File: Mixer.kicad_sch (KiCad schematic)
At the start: 5 parts, among them IC1 ADE-2ASK+, J1 PCB.SMAFRA.HT, J2 PCB.SMAFRA.HT, J3 PCB.SMAFRA.HT

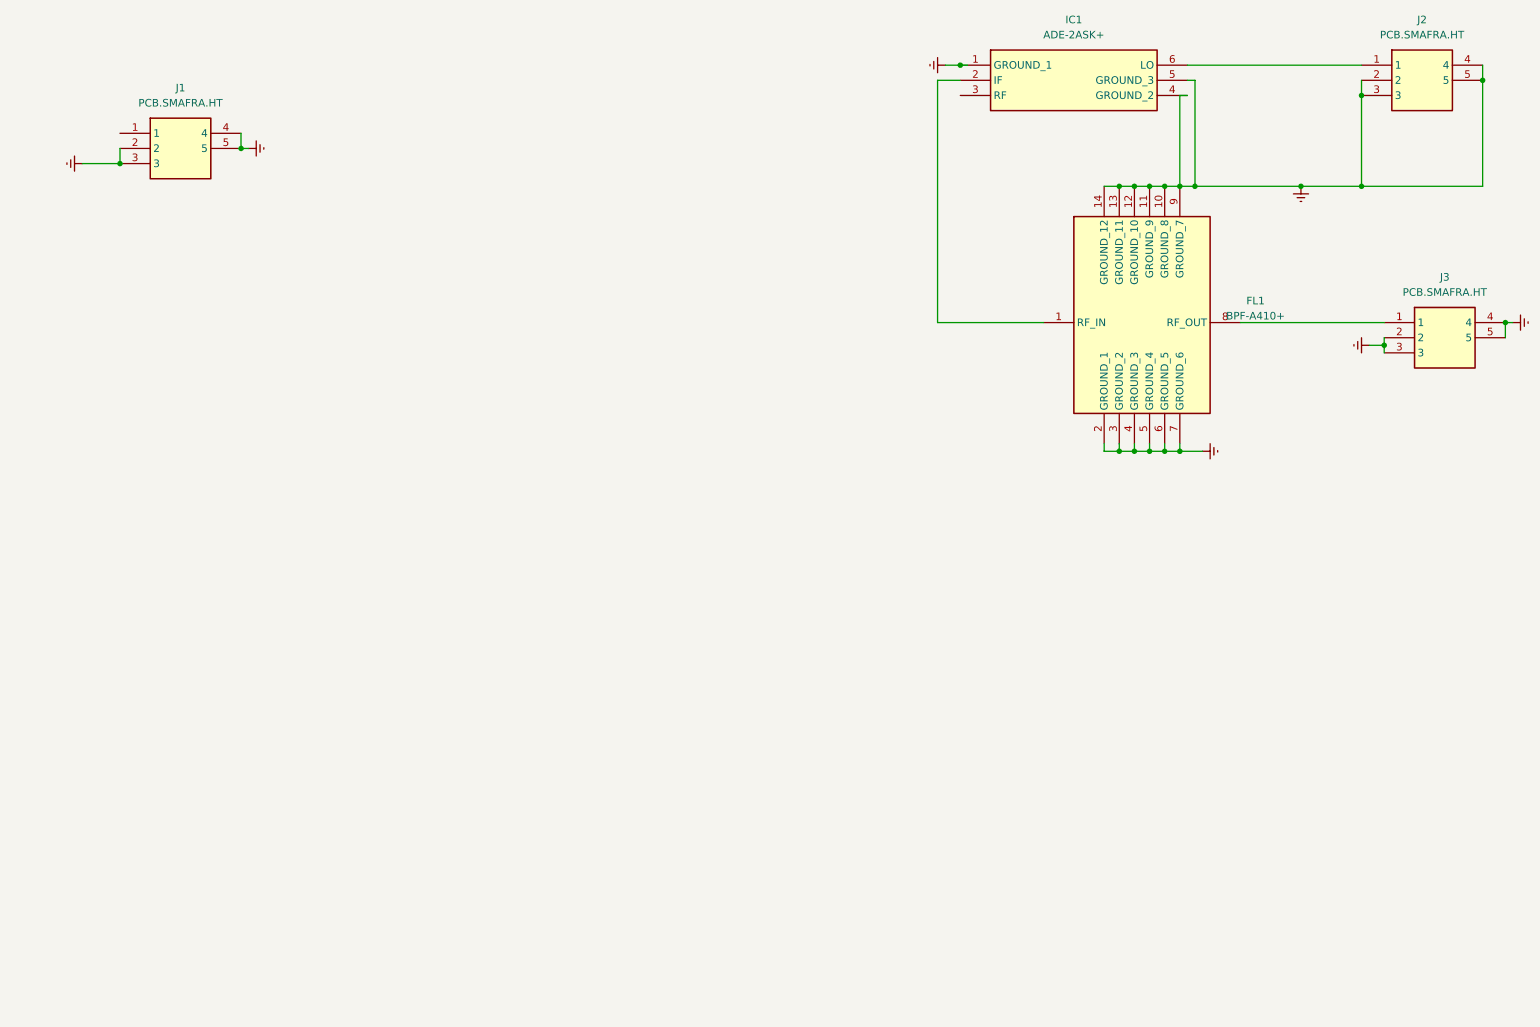
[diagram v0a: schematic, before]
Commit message: Redefined filters & Top Level Diagram
- Implement wider filters to accomodate 10% tolerance parts.
- Break design in to top-level heirarchical blocks.
- Start wiring some of the blocks together.
- Add L-Band segment, but is currently just a copy of the UHF filter.
- Add the start of a TX path.
- Add placeholders for power and band/tune control.
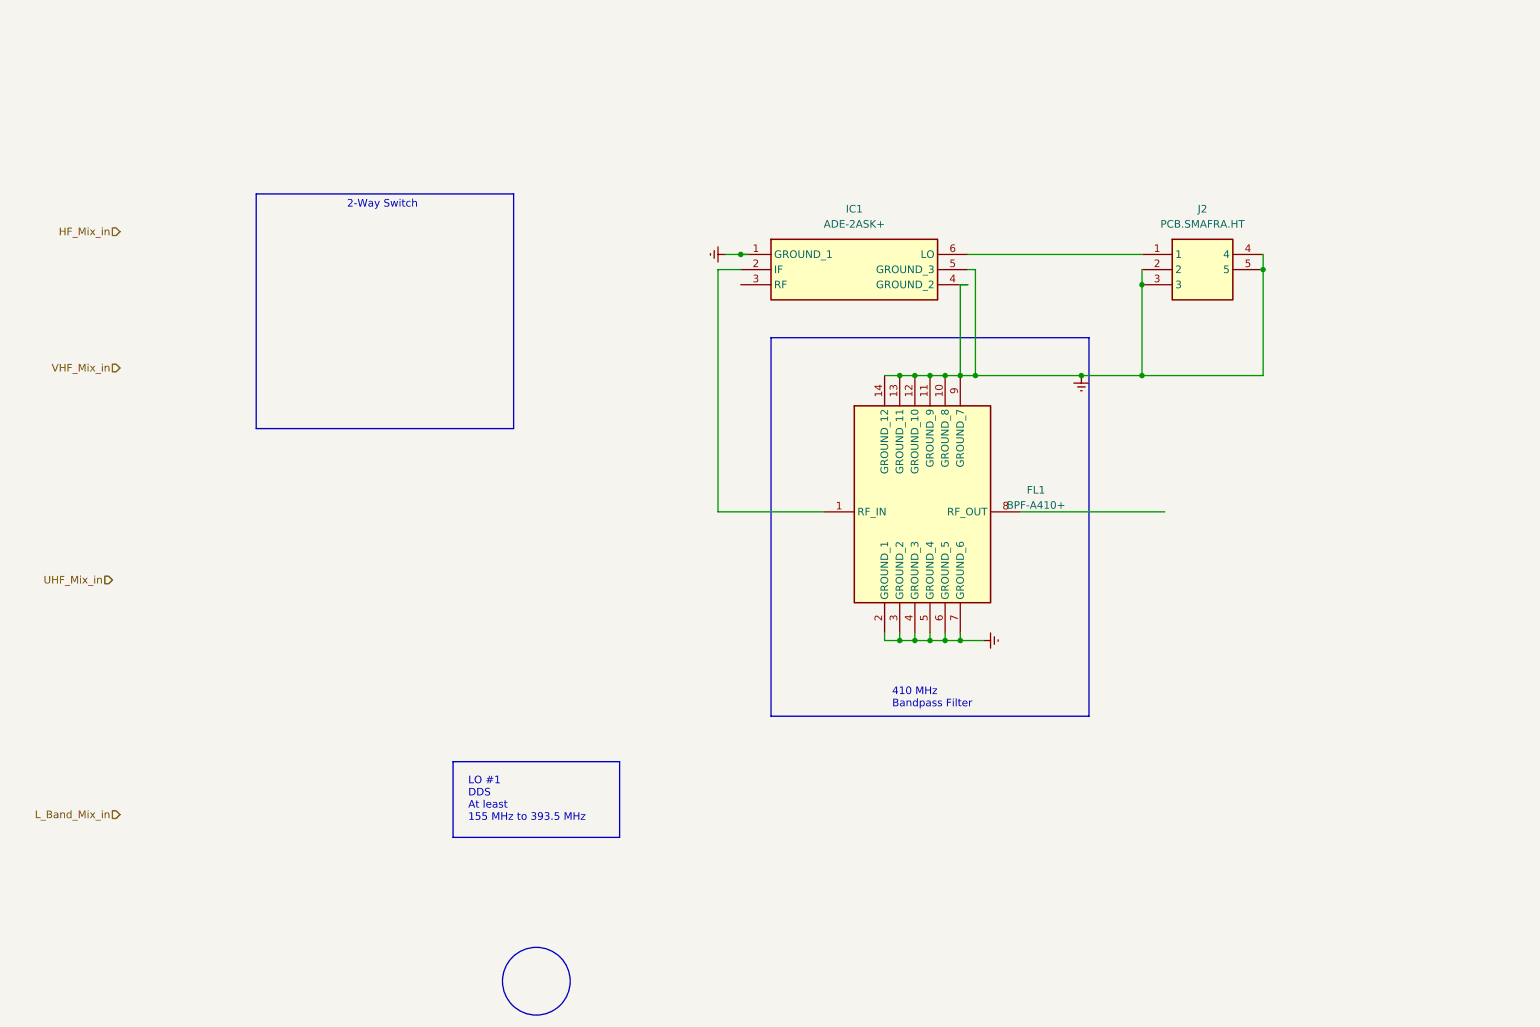
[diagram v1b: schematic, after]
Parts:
- removed J1, J3: PCB.SMAFRA.HT, SamacSys_Parts:PCBSMAFRAHT, symbol SamacSys_Parts:PCB.SMAFRA.HT
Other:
- note added: "2-Way Switch"
- note added: "410 MHz Bandpass Filter"
- note added: "LO #1 DDS At least 155 MHz to 393.5 MHz"
- moved on the sheet: FL1, IC1, J2

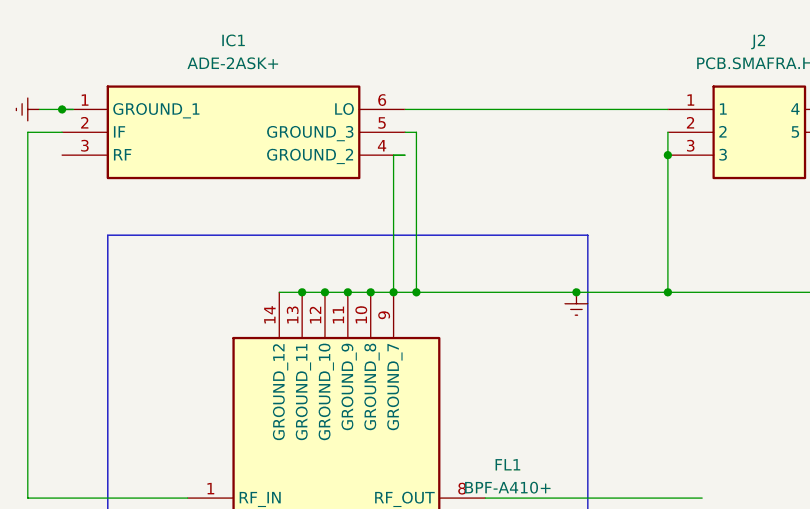
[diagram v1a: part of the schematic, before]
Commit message: More filter work. Add project title to drawings.
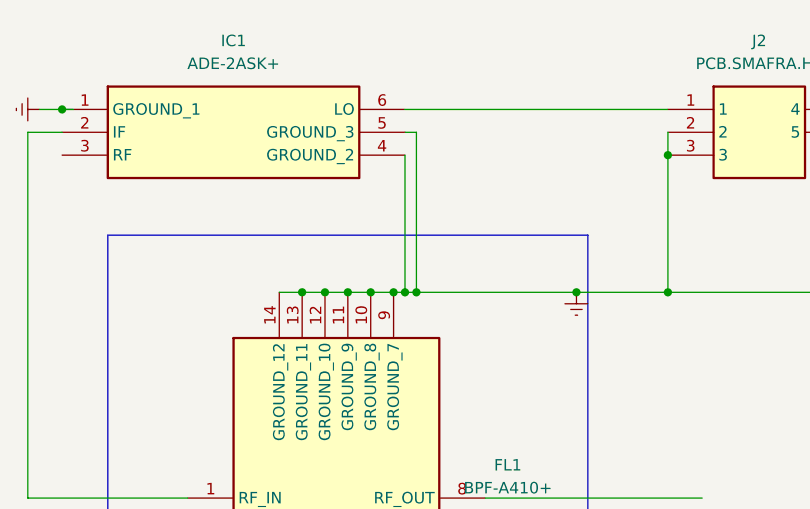
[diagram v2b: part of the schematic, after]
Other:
- company: (none) -> Steves Custom Computers
- title: (none) -> PLUTO RF Card Front-End
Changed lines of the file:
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@@
 (kicad_sch (version 20230121) (generator eeschema)
   (paper "A4")
+  (title_block
+    (title "PLUTO RF Card Front-End")
+    (rev " 001")
+    (company "Steves Custom Computers")
+  )
   (junction (at 170.18 132.08) (diameter 0) (color 0 0 0 0)
   )
@@
   (junction (at 195.58 87.63) (diameter 0) (color 0 0 0 0)
   )
+  (junction (at 176.53 87.63) (diameter 0) (color 0 0 0 0)
+  )
   (junction (at 170.18 87.63) (diameter 0) (color 0 0 0 0)
   )
@@
   )
   (wire (pts (xy 205.74 69.85) (xy 205.74 72.39))
-    (stroke (width 0) (type default))
-  )
-  (wire (pts (xy 175.26 87.63) (xy 177.8 87.63))
     (stroke (width 0) (type default))
   )
@@
     (stroke (width 0) (type default))
   )
-  (wire (pts (xy 175.26 72.39) (xy 176.53 72.39))
-    (stroke (width 0) (type default))
-  )
   (wire (pts (xy 134.62 69.85) (xy 138.43 69.85))
     (stroke (width 0) (type default))
@@
     (stroke (width 0) (type default))
   )
-  (wire (pts (xy 175.26 72.39) (xy 175.26 87.63))
+  (wire (pts (xy 176.53 72.39) (xy 176.53 87.63))
+    (stroke (width 0) (type default))
+  )
+  (wire (pts (xy 176.53 87.63) (xy 177.8 87.63))
     (stroke (width 0) (type default))
   )
@@
     (stroke (width 0) (type default))
   )
+  (wire (pts (xy 176.53 87.63) (xy 175.26 87.63))
+    (stroke (width 0) (type default))
+  )

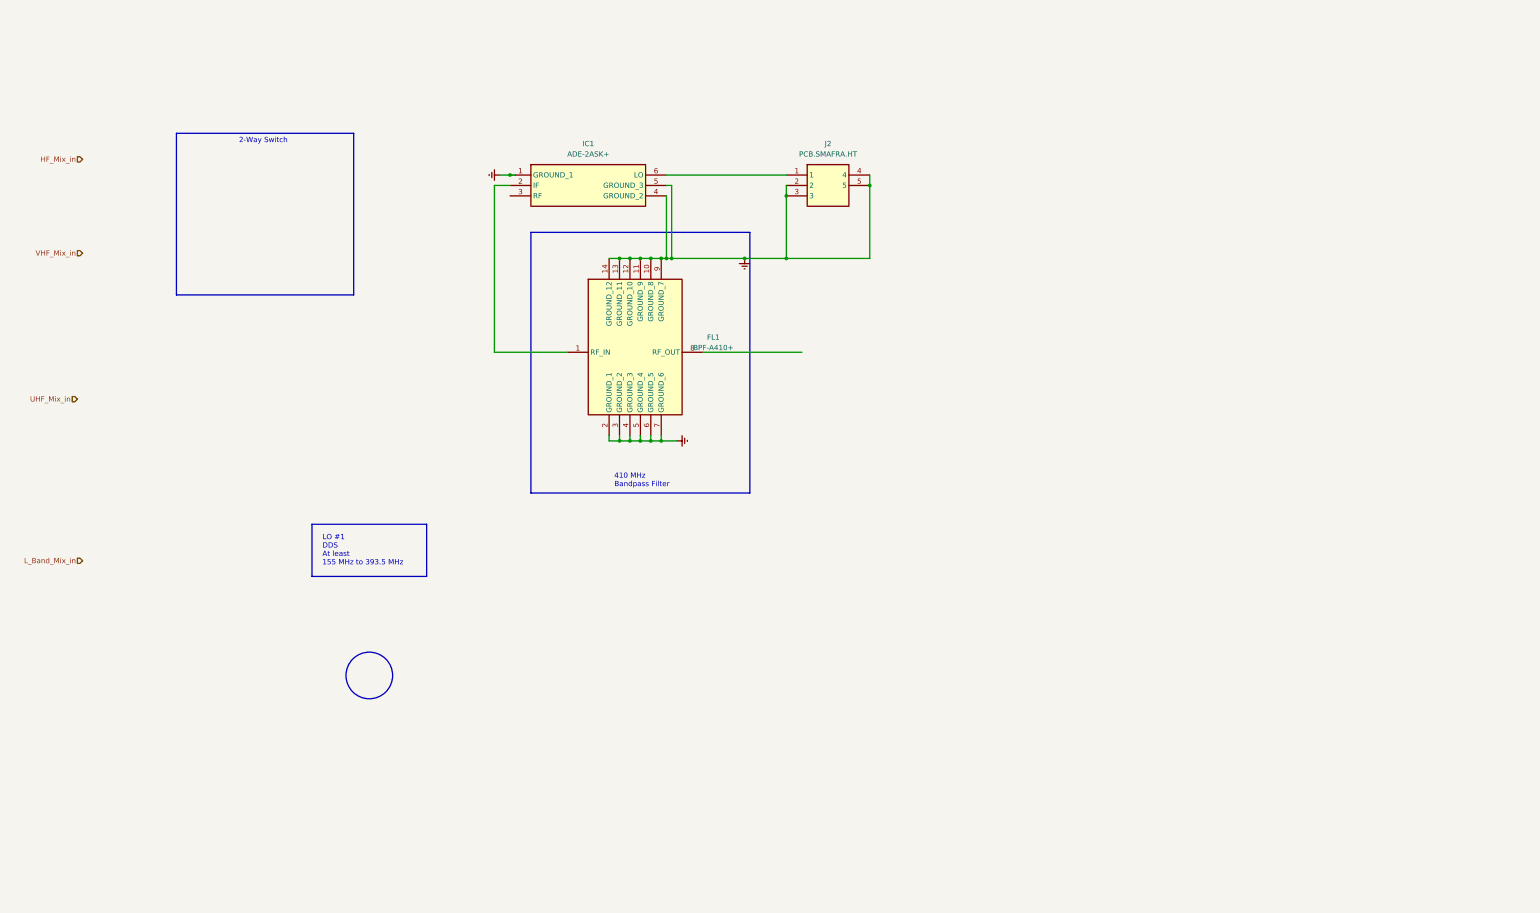
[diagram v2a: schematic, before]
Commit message: Major restructure. Add power/control busses.
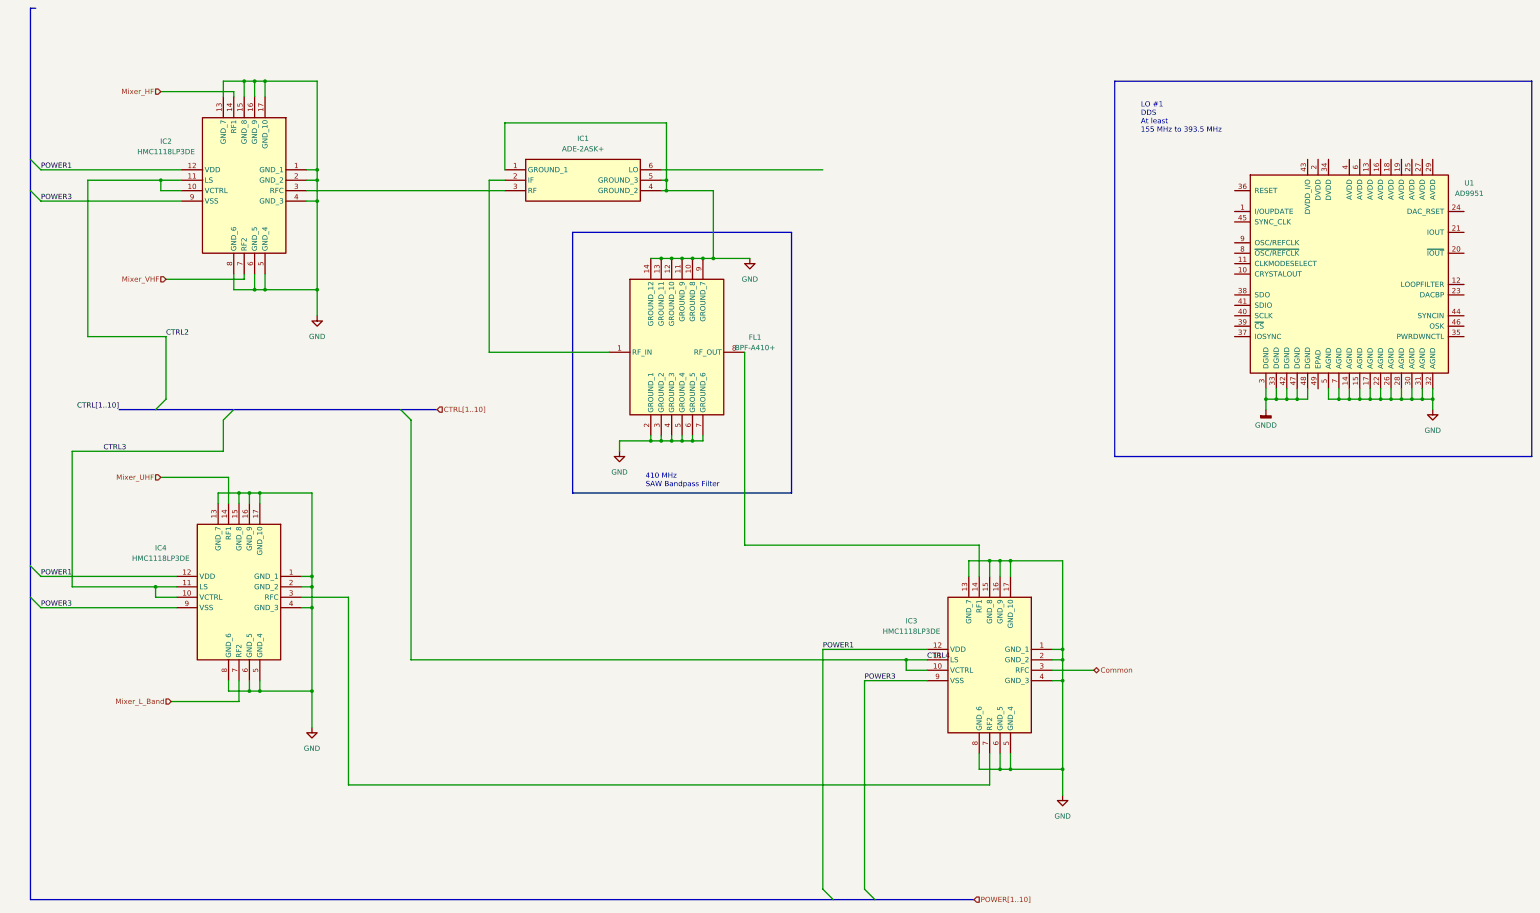
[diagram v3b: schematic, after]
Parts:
- removed FL1: BPF-A410+, SamacSys_Parts:BPFA410, symbol SamacSys_Parts:BPF-A410+
- removed IC1: ADE-2ASK+, SamacSys_Parts:ADE2ASK, symbol SamacSys_Parts:ADE-2ASK+
- removed J2: PCB.SMAFRA.HT, SamacSys_Parts:PCBSMAFRAHT, symbol SamacSys_Parts:PCB.SMAFRA.HT
- added FL1: BPF-A410+, BPFA410, symbol Mouser:BPF-A410+
- added IC1: ADE-2ASK+, ADE2ASK, symbol Mouser:ADE-2ASK+
- added IC2, IC3, IC4: HMC1118LP3DE, QFN50P300X300X95-17N-D, symbol Mouser:HMC1118LP3DE
- added U1: AD9951, Package_QFP:TQFP-48-1EP_7x7mm_P0.5mm_EP3.5x3.5mm, symbol Interface:AD9951
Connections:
- new net: IC3.7 (RF2), IC4.3 (RFC)
- new net: FL1.1 (RF_IN), IC1.2 (IF)
- new net: FL1.8 (RF_OUT), IC3.14 (RF1)
- new net: IC1.3 (RF), IC2.3 (RFC)
- new net CTRL2: IC2.10 (VCTRL), IC2.11 (LS)
- new net CTRL3: IC4.10 (VCTRL), IC4.11 (LS)
- new net CTRL4: IC3.10 (VCTRL), IC3.11 (LS)
- new net Common: IC3.3 (RFC)
- new net GND: FL1.10 (GROUND_8), FL1.11 (GROUND_9), FL1.12 (GROUND_10), FL1.13 (GROUND_11), FL1.14 (GROUND_12), FL1.2 (GROUND_1), FL1.3 (GROUND_2), FL1.4 (GROUND_3), FL1.5 (GROUND_4), FL1.6 (GROUND_5), FL1.7 (GROUND_6), FL1.9 (GROUND_7), IC1.1 (GROUND_1), IC1.4 (GROUND_2), IC1.5 (GROUND_3), IC2.1 (GND_1), IC2.13 (GND_7), IC2.15 (GND_8), IC2.16 (GND_9), IC2.17 (GND_10), IC2.2 (GND_2), IC2.4 (GND_3), IC2.5 (GND_4), IC2.6 (GND_5), IC2.8 (GND_6), IC3.1 (GND_1), IC3.13 (GND_7), IC3.15 (GND_8), IC3.16 (GND_9), IC3.17 (GND_10), IC3.2 (GND_2), IC3.4 (GND_3), IC3.5 (GND_4), IC3.6 (GND_5), IC3.8 (GND_6), IC4.1 (GND_1), IC4.13 (GND_7), IC4.15 (GND_8), IC4.16 (GND_9), IC4.17 (GND_10), IC4.2 (GND_2), IC4.4 (GND_3), IC4.5 (GND_4), IC4.6 (GND_5), IC4.8 (GND_6), U1.14 (AGND), U1.15 (AGND), U1.17 (AGND), U1.22 (AGND), U1.26 (AGND), U1.28 (AGND), U1.30 (AGND), U1.31 (AGND), U1.32 (AGND), U1.5 (AGND), U1.7 (AGND)
- new net GNDD: U1.3 (DGND), U1.33 (DGND), U1.42 (DGND), U1.47 (DGND), U1.48 (DGND)
- new net Mixer_HF: IC2.14 (RF1)
- new net Mixer_L_Band: IC4.7 (RF2)
- new net Mixer_UHF: IC4.14 (RF1)
- new net Mixer_VHF: IC2.7 (RF2)
- new net POWER1: IC2.12 (VDD), IC3.12 (VDD), IC4.12 (VDD)
- new net POWER3: IC2.9 (VSS), IC3.9 (VSS), IC4.9 (VSS)
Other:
- note added: "410 MHz SAW Bandpass Filter"
- note removed: "2-Way Switch"
- note removed: "410 MHz Bandpass Filter"
- title: PLUTO RF Card Front-End -> PLUTO RF Front-End Card

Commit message: Add some of the routing for the power signals.
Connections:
- net POWER1: now also U1.43 (DVDD_I/O)
- net POWER5: now reaches U1.13 (AVDD)
- net POWER5: now also U1.16 (AVDD), U1.18 (AVDD), U1.19 (AVDD), U1.25 (AVDD), U1.27 (AVDD), U1.29 (AVDD), U1.4 (AVDD), U1.6 (AVDD)
- net POWER4: now reaches U1.2 (DVDD)
- net POWER4: now also U1.34 (DVDD)
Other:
- moved on the sheet: U1

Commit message: Replace DDS with VCOs + a switch.
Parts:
- removed U1: AD9951, Package_QFP:TQFP-48-1EP_7x7mm_P0.5mm_EP3.5x3.5mm, symbol Interface:AD9951
- added C2 (x2): 3 pf, Capacitor_SMD:C_1206_3216Metric, symbol Device:C_Small
- added C2 (x4): 1000 pf, Capacitor_SMD:C_1206_3216Metric, symbol Device:C_Small
- added C2 (x2): 1 pf, Capacitor_SMD:C_1206_3216Metric, symbol Device:C_Small
- added IC7: HMC1118LP3DE, QFN50P300X300X95-17N-D, symbol Mouser:HMC1118LP3DE
- added L2 (x3): 68 nH, Inductor_SMD:L_1206_3216Metric, symbol Device:L
- added L2 (x2): 120 nH, Inductor_SMD:L_1206_3216Metric, symbol Device:L
- added L2: 16 nH, Inductor_SMD:L_1206_3216Metric, symbol Device:L
- added R1 (x2): 10 Ohms, Resistor_SMD:R_0805_2012Metric_Pad1.20x1.40mm_HandSolder, symbol Device:R_US
- added R1 (x2): 270 Ohms, Resistor_SMD:R_0805_2012Metric_Pad1.20x1.40mm_HandSolder, symbol Device:R_US
- added Y1: MAX2607EUT+T, SOT95P280X145-6N, symbol Mouser:MAX2607EUT+T
- added Y2: MAX2608EUT+T, SOT95P280X145-6N, symbol Mouser:MAX2608EUT+T
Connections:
- net GND: now also C2.2, C2.2, C2.2, C2.2, IC7.1 (GND_1), IC7.13 (GND_7), IC7.15 (GND_8), IC7.16 (GND_9), IC7.17 (GND_10), IC7.2 (GND_2), IC7.4 (GND_3), IC7.5 (GND_4), IC7.6 (GND_5), IC7.8 (GND_6), L2.2, L2.2, Y1.2 (GND), Y2.2 (GND)
- net POWER1: now also IC7.12 (VDD), R1.1, R1.1
- net POWER3: now also IC7.9 (VSS)
- net at IC1.6 (LO): now also IC7.3 (RFC)
- new net: C2.1, C2.2, C2.2, L2.1, L2.1, R1.2, Y1.5 (VCC)
- new net: C2.1, C2.2, C2.2, L2.1, L2.1, R1.2, Y2.5 (VCC)
- new net: C2.1, R1.1, Y1.3 (TUNE)
- new net: L2.1, Y1.1 (IND)
- new net: C2.1, R1.1, Y2.3 (TUNE)
- new net: C2.1, IC7.7 (RF2)
- new net: C2.1, IC7.14 (RF1)
- new net: L2.2, Y2.4 (OUT-)
- new net: L2.1, Y2.1 (IND)
- new net: L2.2, Y2.6 (OUT+)
- new net: L2.2, Y1.6 (OUT+)
- new net: L2.2, Y1.4 (OUT-)
- new net CTRL7: IC7.10 (VCTRL), IC7.11 (LS)
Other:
- note added: "LO: At least 155 MHz to 393.5 MHz"
- note removed: "LO #1 DDS At least 155 MHz to 393.5 MHz"
